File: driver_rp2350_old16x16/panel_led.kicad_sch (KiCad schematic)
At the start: 342 parts

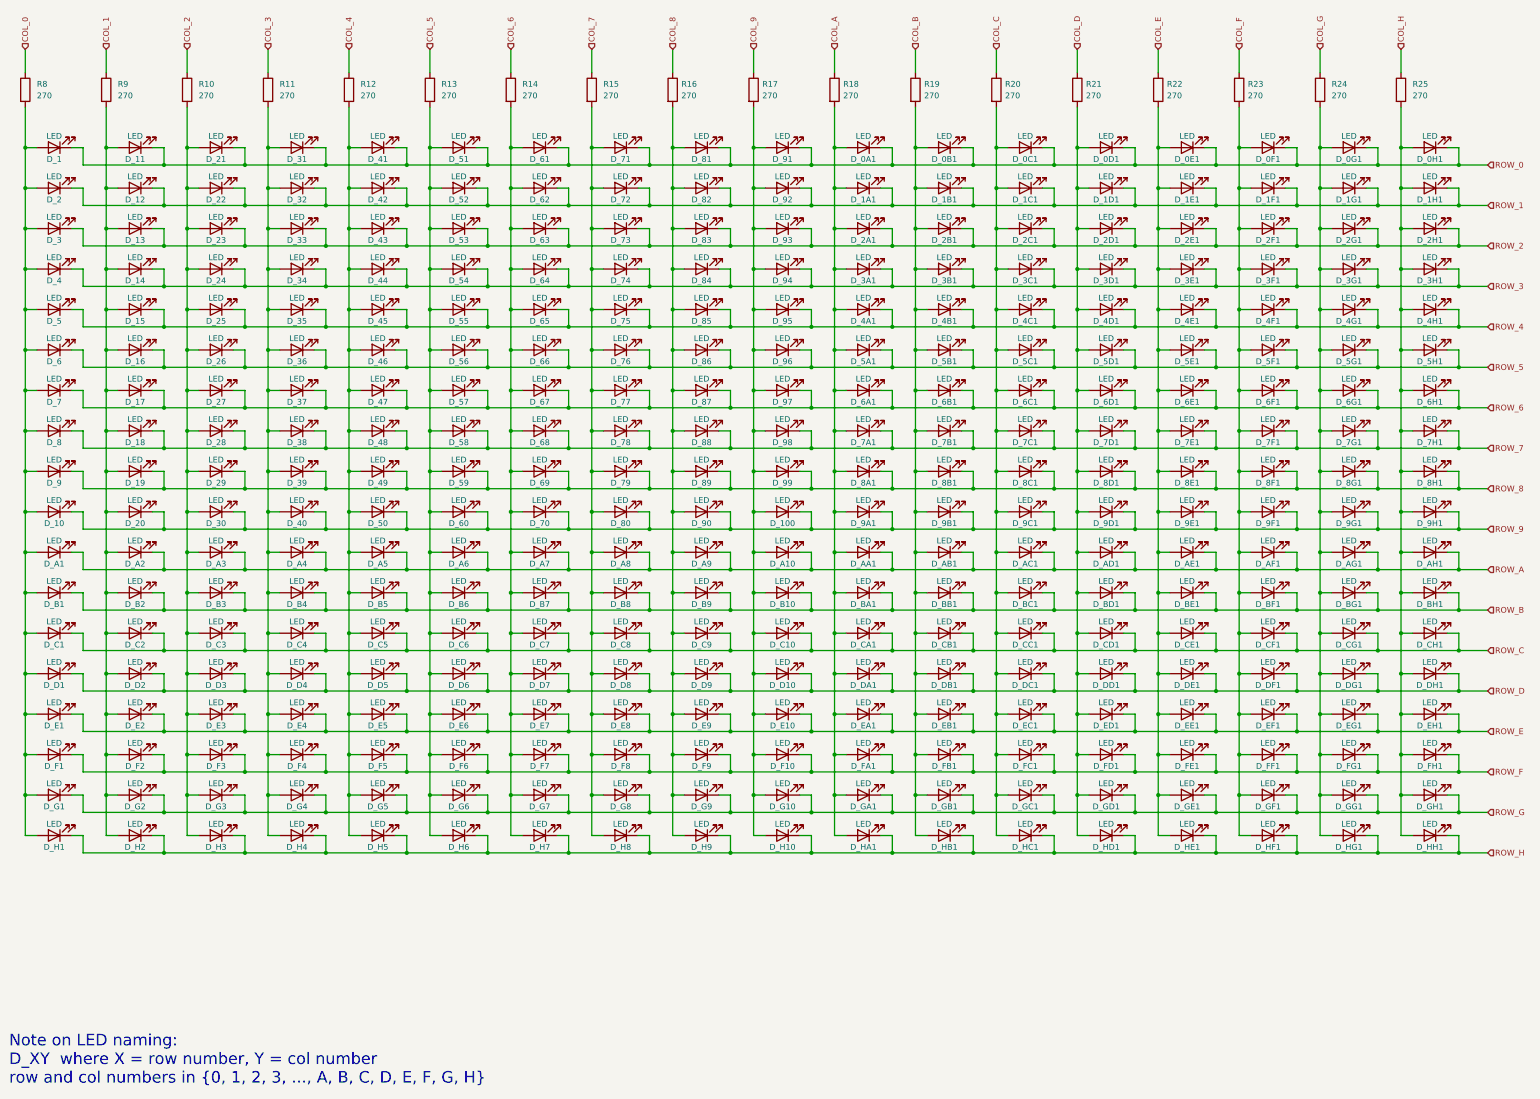
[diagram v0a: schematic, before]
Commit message: Worked on new 18x18 led version of rp2350 design.
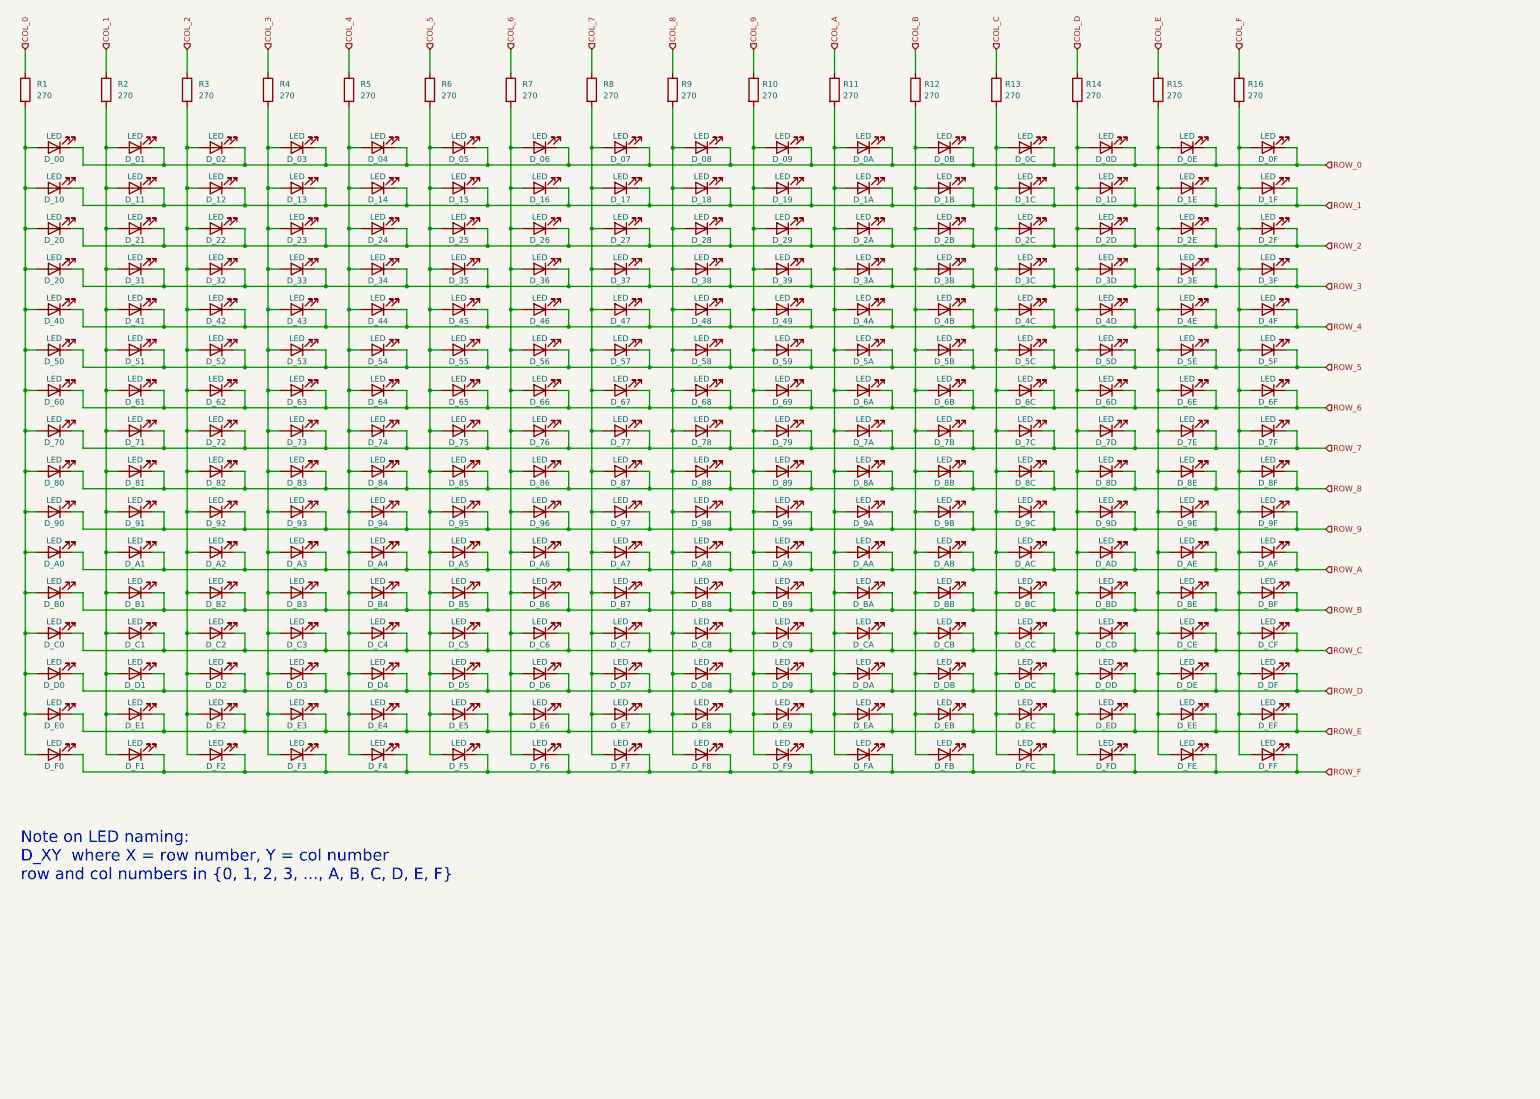
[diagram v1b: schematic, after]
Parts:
- removed D_0G1, D_0H1, D_1G1, D_1H1, D_2G1, D_2H1, D_3G1, D_3H1, D_4G1, D_4H1, D_5G1, D_5H1, D_6G1, D_6H1, D_7G1, D_7H1, D_8G1, D_8H1, D_9G1, D_9H1, D_AG1, D_AH1, D_BG1, D_BH1, D_CG1, D_CH1, D_DG1, D_DH1, D_EG1, D_EH1, D_FG1, D_FH1, D_G1, D_G10, D_G2, D_G3, D_G4, D_G5, D_G6, D_G7, D_G8, D_G9, D_GA1, D_GB1, D_GC1, D_GD1, D_GE1, D_GF1, D_GG1, D_GH1, D_H1, D_H10, D_H2, D_H3, D_H4, D_H5, D_H6, D_H7, D_H8, D_H9, D_HA1, D_HB1, D_HC1, D_HD1, D_HE1, D_HF1, D_HG1, D_HH1: LED, panel_custom:LED_0402_1005Metric, symbol Device:LED
- removed R24, R25: 270, symbol Device:R
- R1: renamed from R8; footprint panel_custom:JST_SH_BM04B-SRSS-TB_1x04-1MP_P1.00mm_Vertical -> (none)
- renumbered D_1 to D_00, D_11 to D_01, D_21 to D_02, D_31 to D_03, D_41 to D_04, D_51 to D_05, D_61 to D_06, D_71 to D_07, D_81 to D_08, D_91 to D_09, D_0A1 to D_0A, D_0B1 to D_0B, D_0C1 to D_0C, D_0D1 to D_0D, D_0E1 to D_0E, D_0F1 to D_0F, D_2 to D_10, D_12 to D_11, D_22 to D_12, D_32 to D_13, D_42 to D_14, D_52 to D_15, D_62 to D_16, D_72 to D_17, D_82 to D_18, D_92 to D_19, D_1A1 to D_1A, D_1B1 to D_1B, D_1C1 to D_1C, D_1D1 to D_1D, D_1E1 to D_1E, D_1F1 to D_1F, D_3 to D_20, D_4 to D_20, D_13 to D_21, D_23 to D_22, D_33 to D_23, D_43 to D_24, D_53 to D_25, D_63 to D_26, D_73 to D_27, D_83 to D_28, D_93 to D_29, D_2A1 to D_2A, D_2B1 to D_2B, D_2C1 to D_2C, D_2D1 to D_2D, D_2E1 to D_2E, D_2F1 to D_2F, D_14 to D_31, D_24 to D_32, D_34 to D_33, D_44 to D_34, D_54 to D_35, D_64 to D_36, D_74 to D_37, D_84 to D_38, D_94 to D_39, D_3A1 to D_3A, D_3B1 to D_3B, D_3C1 to D_3C, D_3D1 to D_3D, D_3E1 to D_3E, D_3F1 to D_3F, D_5 to D_40, D_15 to D_41, D_25 to D_42, D_35 to D_43, D_45 to D_44, D_55 to D_45, D_65 to D_46, D_75 to D_47, D_85 to D_48, D_95 to D_49, D_4A1 to D_4A, D_4B1 to D_4B, D_4C1 to D_4C, D_4D1 to D_4D, D_4E1 to D_4E, D_4F1 to D_4F, D_6 to D_50, D_16 to D_51, D_26 to D_52, D_36 to D_53, D_46 to D_54, D_56 to D_55, D_66 to D_56, D_76 to D_57, D_86 to D_58, D_96 to D_59, D_5A1 to D_5A, D_5B1 to D_5B, D_5C1 to D_5C, D_5D1 to D_5D, D_5E1 to D_5E, D_5F1 to D_5F, D_7 to D_60, D_17 to D_61, D_27 to D_62, D_37 to D_63, D_47 to D_64, D_57 to D_65, D_67 to D_66, D_77 to D_67, D_87 to D_68, D_97 to D_69, D_6A1 to D_6A, D_6B1 to D_6B, D_6C1 to D_6C, D_6D1 to D_6D, D_6E1 to D_6E, D_6F1 to D_6F, D_8 to D_70, D_18 to D_71, D_28 to D_72, D_38 to D_73, D_48 to D_74, D_58 to D_75, D_68 to D_76, D_78 to D_77, D_88 to D_78, D_98 to D_79, D_7A1 to D_7A, D_7B1 to D_7B, D_7C1 to D_7C, D_7D1 to D_7D, D_7E1 to D_7E, D_7F1 to D_7F, D_9 to D_80, D_19 to D_81, D_29 to D_82, D_39 to D_83, D_49 to D_84, D_59 to D_85, D_69 to D_86, D_79 to D_87, D_89 to D_88, D_99 to D_89, D_8A1 to D_8A, D_8B1 to D_8B, D_8C1 to D_8C, D_8D1 to D_8D, D_8E1 to D_8E, D_8F1 to D_8F, D_10 to D_90, D_20 to D_91, D_30 to D_92, D_40 to D_93, D_50 to D_94, D_60 to D_95, D_70 to D_96, D_80 to D_97, D_90 to D_98, D_100 to D_99, D_9A1 to D_9A, D_9B1 to D_9B, D_9C1 to D_9C, D_9D1 to D_9D, D_9E1 to D_9E, D_9F1 to D_9F, D_A1 to D_A0, D_A2 to D_A1, D_A3 to D_A2, D_A4 to D_A3, D_A5 to D_A4, D_A6 to D_A5, D_A7 to D_A6, D_A8 to D_A7, D_A9 to D_A8, D_A10 to D_A9, D_AA1 to D_AA, D_AB1 to D_AB, D_AC1 to D_AC, D_AD1 to D_AD, D_AE1 to D_AE, D_AF1 to D_AF, D_B1 to D_B0, D_B2 to D_B1, D_B3 to D_B2, D_B4 to D_B3, D_B5 to D_B4, D_B6 to D_B5, D_B7 to D_B6, D_B8 to D_B7, D_B9 to D_B8, D_B10 to D_B9, D_BA1 to D_BA, D_BB1 to D_BB, D_BC1 to D_BC, D_BD1 to D_BD, D_BE1 to D_BE, D_BF1 to D_BF, D_C1 to D_C0, D_C2 to D_C1, D_C3 to D_C2, D_C4 to D_C3, D_C5 to D_C4, D_C6 to D_C5, D_C7 to D_C6, D_C8 to D_C7, D_C9 to D_C8, D_C10 to D_C9, D_CA1 to D_CA, D_CB1 to D_CB, D_CC1 to D_CC, D_CD1 to D_CD, D_CE1 to D_CE, D_CF1 to D_CF, D_D1 to D_D0, D_D2 to D_D1, D_D3 to D_D2, D_D4 to D_D3, D_D5 to D_D4, D_D6 to D_D5, D_D7 to D_D6, D_D8 to D_D7, D_D9 to D_D8, D_D10 to D_D9, D_DA1 to D_DA, D_DB1 to D_DB, D_DC1 to D_DC, D_DD1 to D_DD, D_DE1 to D_DE, D_DF1 to D_DF, D_E1 to D_E0, D_E2 to D_E1, D_E3 to D_E2, D_E4 to D_E3, D_E5 to D_E4, D_E6 to D_E5, D_E7 to D_E6, D_E8 to D_E7, D_E9 to D_E8, D_E10 to D_E9, D_EA1 to D_EA, D_EB1 to D_EB, D_EC1 to D_EC, D_ED1 to D_ED, D_EE1 to D_EE, D_EF1 to D_EF, D_F1 to D_F0, D_F2 to D_F1, D_F3 to D_F2, D_F4 to D_F3, D_F5 to D_F4, D_F6 to D_F5, D_F7 to D_F6, D_F8 to D_F7, D_F9 to D_F8, D_F10 to D_F9, D_FA1 to D_FA, D_FB1 to D_FB, D_FC1 to D_FC, D_FD1 to D_FD, D_FE1 to D_FE, D_FF1 to D_FF, R17 to R10, R18 to R11, R19 to R12, R20 to R13, R21 to R14, R22 to R15, R23 to R16, R9 to R2, R10 to R3, R11 to R4, R12 to R5, R13 to R6, R14 to R7, R15 to R8, R16 to R9
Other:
- note added: "Note on LED naming: D_XY where X = row number, Y = col number row and col numbers in {0, 1, 2, 3, ..., A, B, C, D, E, F}"
- note removed: "Note on LED naming: D_XY where X = row number, Y = col number row and col numbers in {0, 1, 2, 3, ..., A, B, C, D, E, F, G, H}"
